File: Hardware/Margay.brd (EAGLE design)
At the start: 50.2 x 30.4 mm, 71 parts, among them IC1 ATMEGA644M, J1 CONN_42.54_SCREW, J2 CONN_6SCREW_2.54, Q1 FDN360P, Q2 DMG3404, Q3 2N7002, Q4 FDN360P, Q6 FDN360P, U2 FT231X-Q

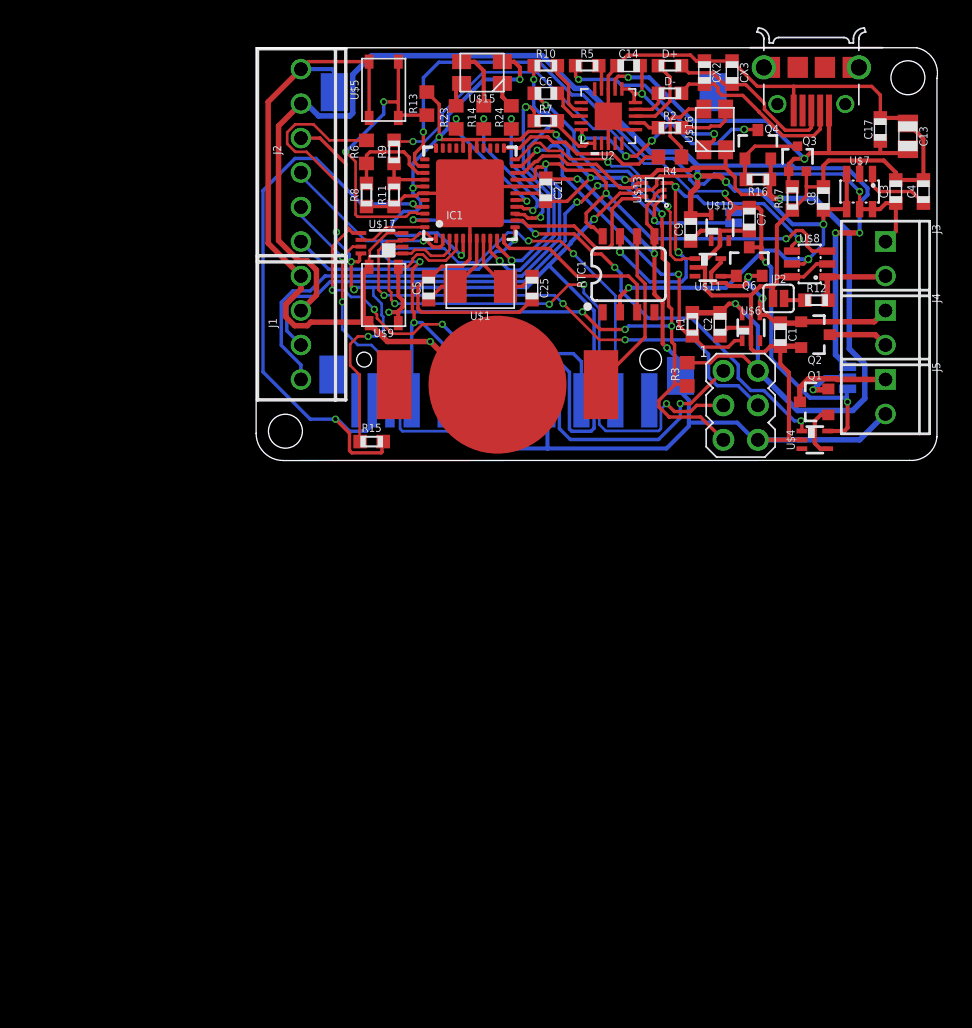
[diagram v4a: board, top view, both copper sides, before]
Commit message: First round of v2 updates to schematic
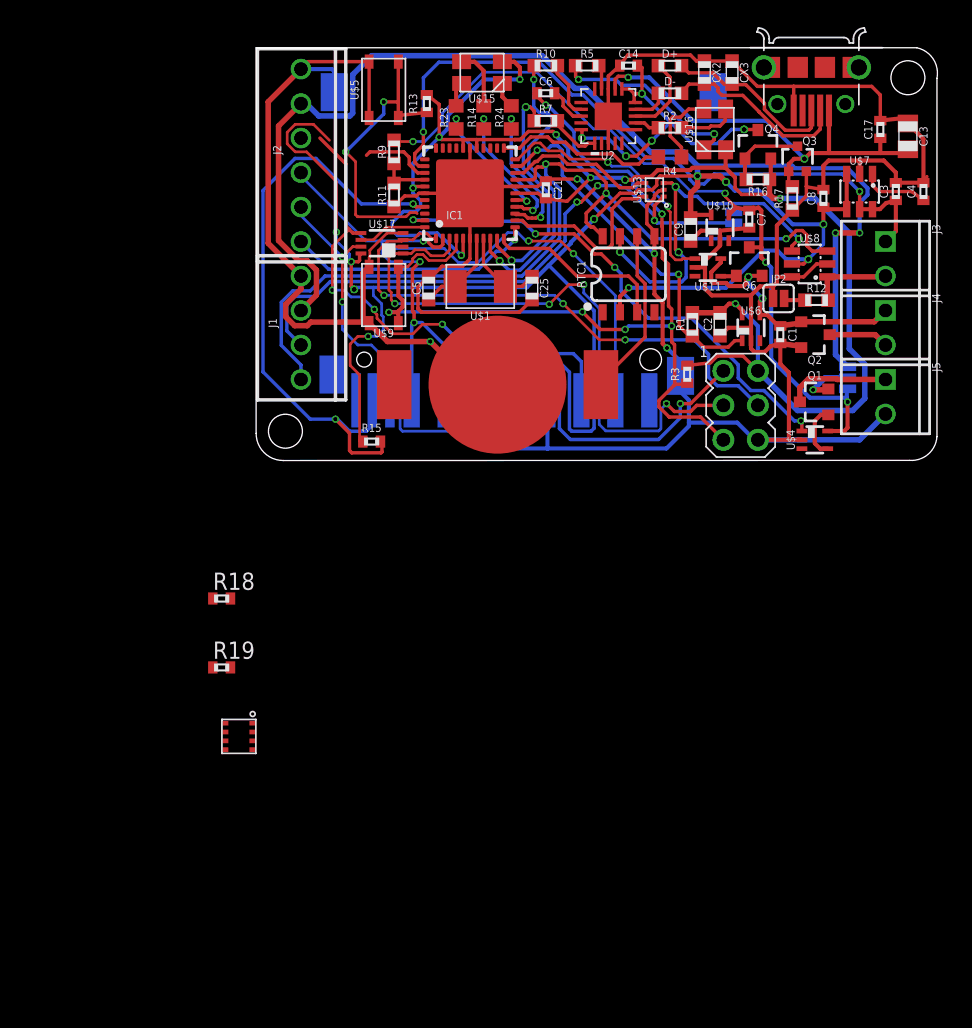
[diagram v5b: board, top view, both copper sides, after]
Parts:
- removed R6: (no value), bschulz:R0603
- removed R8: (no value), bschulz_passives:R0603
- added R18, R19: 4.7k, bschulz_passives:R0402
- added U$12: BME280, bschulz:BME280
- C1, C14, C17, C21, C3, C4, C6, C7, C8: device bschulz_passives:C0603 -> bschulz_passives:C0402
- R13, R3: device bschulz:R0603 -> bschulz_passives:R0402
- R15: device bschulz_passives:R0603 -> bschulz_passives:R0402
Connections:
- new net ADC_EXT: IC1.34, J2.5
- new net RX_EXT: IC1.11, J2.4
- new net TX_EXT: IC1.12, J2.3
- net 3V3_AUX: now also R18.2, R19.2, U$12.2, U$12.5, U$12.6, U$12.8; no longer R6.2
- net EXT_INT: no longer IC1.12
- net GND: now also U$12.1, U$12.7; no longer R8.1
- net LOG_INT: now also IC1.33; no longer IC1.42
- net MISO: no longer J2.4
- net MOSI_BUF: no longer J2.3
- net RTC_INT: now also IC1.42; no longer IC1.11
- net SCK_BUF: no longer J2.5
- net SCL: now also R19.1, U$12.4
- net SDA: now also R18.1
- net SDA_OB: now also U$12.3
- net THERM_SENSE: no longer R6.1, R8.2
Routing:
- net 3V3_AUX: track 217.8 -> 215.6 mm
- net THERM_SENSE: track 7.42 -> 5.35 mm
- net MOSI_BUF: track 39.2 -> 37.8 mm
- net GND: track 279.4 -> 278.5 mm
- net SCK_BUF: track 29.8 -> 29.2 mm
- net LOG_INT: track 22.8 -> 22.2 mm

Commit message: Revised schematic for Margay v2, added circuit simulations
Will remove some simulations later, still need to do much layout and placement, as well as verify the schematic
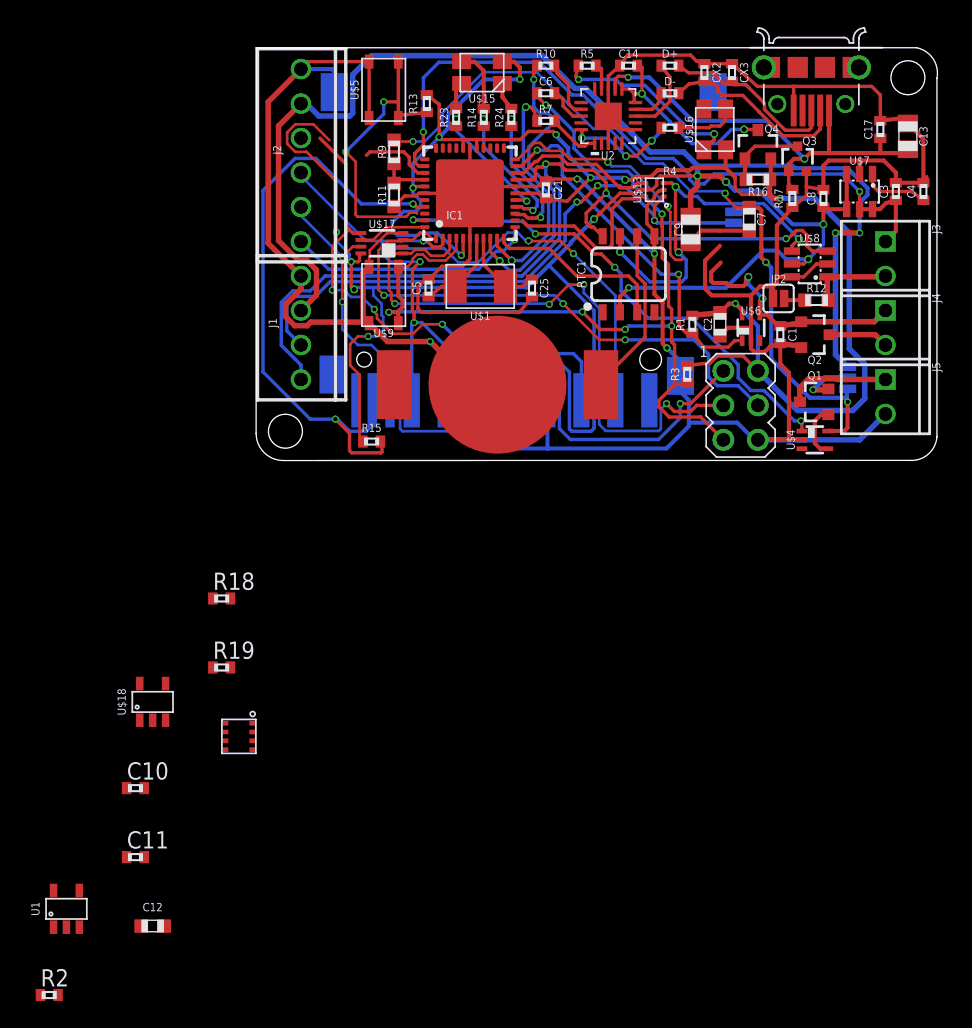
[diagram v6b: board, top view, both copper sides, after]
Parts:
- removed Q6: FDN360P, bschulz:SOT23-3
- removed U$10: TPS79733, bschulz:DCK_R-PDSO-G5
- removed U$11: MIC842H, bschulz:DCK_R-PDSO-G5
- added C10, C11: 0.1uF, bschulz_passives:C0402
- added C12: 1uF, bschulz_passives:C0603
- added U$18: TPS2105, bschulz:SOT23-5
- added U1: TPS7A0533DBV, bschulz:SOT23-5
- C25, C5, CX2, CX3: device bschulz_passives:C0603 -> bschulz_passives:C0402
- C7: value 0.1uF -> 1uF; device bschulz_passives:C0402 -> bschulz_passives:C0603
- C9: value 1uF -> 10uF; device bschulz_passives:C0603 -> bschulz_passives:C0805
- D+, D-, R1, R10, R17, R4, R5, R7: device bschulz_passives:R0603 -> bschulz_passives:R0402
- R14, R2, R23, R24: device bschulz:R0603 -> bschulz_passives:R0402
- moved R2 76.8 mm to (-15.2, -39.4)
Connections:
- removed net EXT_INT: J2.6
- removed net N$4 (its old number): Q6.1, U$11.4
- new net GPIO_EXT: IC1.13, J2.6
- new net SDA_CTRL: IC1.24, U$13.6
- net 3V3_AUX: now also U1.5; no longer U$10.5
- net 3V3_AUX_CTRL: now also IC1.25, U1.3; no longer IC1.13, U$13.6
- net ALIVE_LED: no longer U$16.4
- net GND: now also C10.2, C11.2, C12.2, U$18.2, U1.2; no longer U$10.2, U$11.2
- net N$1: now also U$16.4; no longer IC1.23
- net VBAT+: now also C10.1, U$18.5; no longer Q6.2, U$11.5
- net VBAT_SW: now also C12.1, U$18.4, U1.1; no longer Q6.3, U$10.4
- net VBAT_SW_CTRL: now also U$18.1; no longer U$11.1
- net VUSB: now also C11.1, U$18.3
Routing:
- net GPIO_EXT: track 0.00 -> 18.4 mm, vias 0 -> 1
- net EXT_INT: track 18.4 -> 0.00 mm, vias 1 -> 0
- net 3V3_AUX_CTRL: track 13.6 -> 0.00 mm
- net SDA_CTRL: track 0.00 -> 13.0 mm
- net N$1: track 12.8 -> 0.00 mm
- net ALIVE_LED: track 5.91 -> 0.00 mm
- net N$4: track 1.84 -> 0.00 mm
- net VBAT_SW: track 58.9 -> 57.2 mm
- net GND: track 278.5 -> 276.8 mm
- net 3V3_AUX: track 215.6 -> 214.1 mm
- net VBAT+: track 19.9 -> 18.7 mm
- net N$4 (its old number): track 1.16 -> 0.00 mm
- net VBAT_SW_CTRL: track 19.4 -> 18.5 mm

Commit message: Begining of v2 layout
Power section and severl problematic signals taken care of, still need to add BME280 and fix header connections
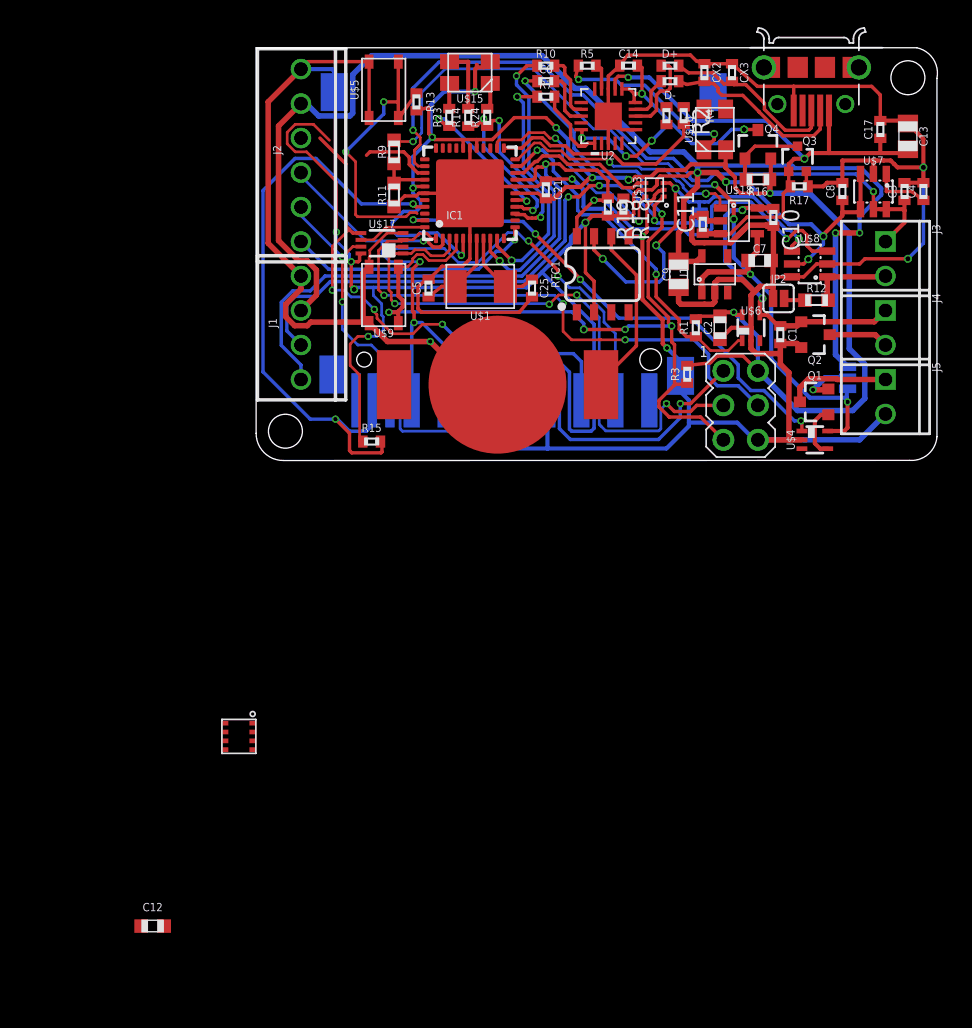
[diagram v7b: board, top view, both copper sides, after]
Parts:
- moved R2 79.9 mm to (31.5, 25.4), turned to 270 degrees
- moved U1 66.8 mm to (33.8, 13.7)
- moved C10 63.0 mm to (38.1, 17.9), turned to 270 degrees
- moved C11 62.6 mm to (32.9, 17.4), turned to 90 degrees
- moved U$18 55.9 mm to (35.6, 17.7), turned to 270 degrees
- moved R19 44.3 mm to (25.9, 18.7), turned to 270 degrees
- moved R18 41.3 mm to (27.1, 18.7), turned to 270 degrees
- moved C9 3.42 mm to (31.1, 13.7)
- moved C7 3.14 mm to (37.1, 14.7), turned to 0 degrees
- moved JP3 2.54 mm to (32.6, 17.9)
- moved RTC1 1.90 mm to (25.5, 13.7)
- moved R7 1.78 mm to (21.3, 26.8)
- moved R24 1.78 mm to (17.0, 25.3)
- moved C8 1.49 mm to (43.2, 19.8)
- moved R14 1.14 mm to (15.6, 25.3)
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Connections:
- net ALIVE_LED: now also IC1.23
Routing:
- net GND: track 276.8 -> 295.6 mm, vias 4 -> 6
- net ALIVE_LED: track 0.00 -> 16.1 mm
- net RTC_INT: track 13.1 -> 0.00 mm
- net VUSB: track 32.7 -> 41.3 mm
- net VBAT_SW: track 57.2 -> 65.7 mm, vias 4 -> 5
- net N$26: track 4.51 -> 0.05 mm
- net SCL: track 66.9 -> 71.2 mm
- net VBAT+: track 18.7 -> 22.8 mm
- net SDA_CTRL: track 13.0 -> 16.4 mm, vias 0 -> 2
- net RST: track 68.9 -> 72.2 mm
- net VREF: track 52.2 -> 54.4 mm
- net N$35: track 3.95 -> 6.01 mm
- net SDA_EXT: track 44.5 -> 42.5 mm
- net 3V3: track 117.1 -> 115.6 mm
- net SCK: track 46.3 -> 44.9 mm
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
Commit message: Main v2 layout complete, needs review minor cleanup
Main layout is completed, needs verification and review for any traces which need to be cleaned up. Double check power on schematic!
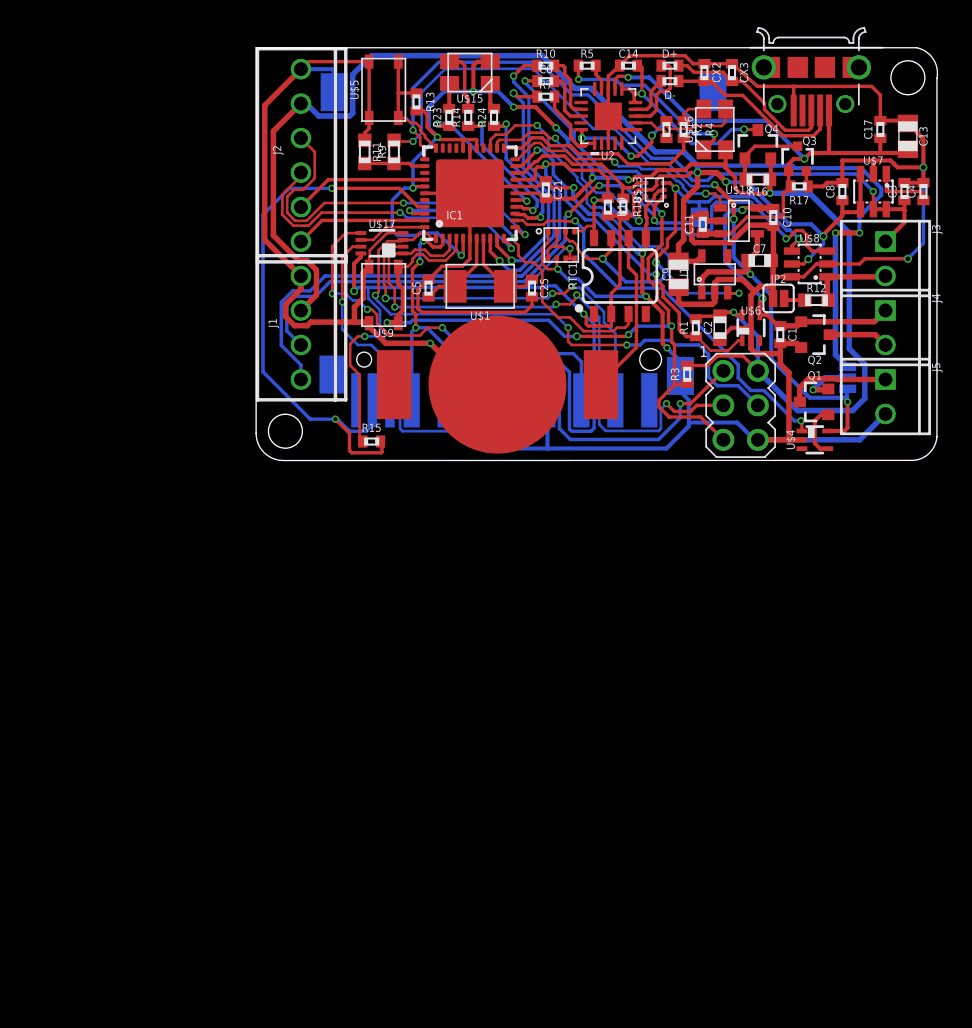
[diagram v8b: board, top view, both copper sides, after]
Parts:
- removed C12: 1uF, bschulz_passives:C0603
- moved U$12 43.3 mm to (22.5, 15.9), turned to 90 degrees
- moved R11 3.84 mm to (8.00, 22.7), turned to 270 degrees
- moved RTC1 1.28 mm to (26.8, 13.6)
- moved R2 1.02 mm to (31.5, 24.4)
- moved R4 1.02 mm to (30.2, 24.4)
- moved R24 0.51 mm to (17.5, 25.3)
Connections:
- net ADC_EXT: now also IC1.37; no longer IC1.34
- net BAT_SENSE: now also IC1.35; no longer IC1.37
- net GND: no longer C12.2
- net GPIO_EXT: now also IC1.43; no longer IC1.13
- net VBAT_SW: no longer C12.1
- net VREF: now also IC1.34; no longer IC1.35
- net VSWITCH_CTRL: now also IC1.13; no longer IC1.43
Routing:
- net TX_EXT: track 0.00 -> 27.4 mm, vias 0 -> 2
- net 3V3_AUX_CTRL: track 0.00 -> 27.3 mm, vias 0 -> 2
- net RTC_INT: track 0.00 -> 23.9 mm, vias 0 -> 2
- net RX_EXT: track 0.00 -> 23.3 mm, vias 0 -> 2
- net MISO: track 67.8 -> 54.3 mm
- net LOG_INT: track 22.3 -> 9.55 mm, vias 2 -> 0
- net GND: track 295.6 -> 305.6 mm, vias 6 -> 8
- net ADC_EXT: track 0.00 -> 9.96 mm
- net 3V3_AUX: track 213.3 -> 203.5 mm, vias 11 -> 10
- net GPIO_EXT: track 18.4 -> 9.77 mm, vias 1 -> 0
- net MOSI_BUF: track 37.8 -> 30.1 mm
- net VSWITCH_CTRL: track 36.9 -> 29.8 mm, vias 4 -> 2
- net N$26: track 0.05 -> 5.99 mm
- net THERM_SENSE: track 5.35 -> 0.00 mm
- net SCK_BUF: track 29.2 -> 24.8 mm, vias 2 -> 1
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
